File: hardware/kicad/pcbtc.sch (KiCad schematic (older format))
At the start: 93 parts, among them J1 USB_C_Receptacle_USB2.0, J4 XT60, Q2 LMG5200, Q3 IPD50R380CE, Q4 LMG5200, SW1 Setup, T1 Transformer_1P_1S_0, U1 USBLC6-4SC6, U10 74LVC1G11, U11 USBLC6-4SC6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

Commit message: pretty schematics
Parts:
- removed R17: 10, Resistor_SMD:R_0603_1608Metric, symbol Device:R
- added R17: 10, symbol Device:R_Small
- added R?: 5k1, Resistor_SMD:R_0603_1608Metric, symbol Device:R_Small
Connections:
- net GNDD: now also R?.2
- net at Q3.1 (G): now also R17.1
- net at U7.2 (GATE): now also R17.2
- net FLYBACK renamed BOOST
- net BOOST: now also R?.1
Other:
- note added: "DCDC feedback"
- note added: "Dead time generator"
- note added: "Feedback recovery"
- note added: "Flyback boost converter"
- note added: "GaN full bridge"
- note added: "STM32 control"
- note added: "USB Vin"
- note added: "USB current measurement"
- moved on the sheet: C1, C10, C11, C12, C13, C14, C15, C16, C17, C18, C19, C2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

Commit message: Released V1.6 gerber
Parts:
- removed JP1: Boot, Jumper:SolderJumper-2_P1.3mm_Open_RoundedPad1.0x1.5mm, symbol Jumper:SolderJumper_2_Open
- removed R7: 2k, Resistor_SMD:R_0603_1608Metric, symbol Device:R
- added C32: 10u, Capacitor_SMD:C_0603_1608Metric, symbol Device:C_Small
- added C33, C40: 10u, Capacitor_SMD:C_1206_3216Metric, symbol Device:C
- added C39, C42: 470pF, Capacitor_SMD:C_1206_3216Metric, symbol Device:C
- added C41: 100n, Capacitor_SMD:C_1206_3216Metric, symbol Device:C
- added C43, C44: 10u, Capacitor_SMD:C_0603_1608Metric, symbol Device:C
- added R15: 120, Resistor_SMD:R_0603_1608Metric, symbol Device:R
- C34: value 1n -> 100n; footprint Capacitor_SMD:C_0603_1608Metric -> Capacitor_SMD:C_1206_3216Metric
- JP2: footprint Jumper:SolderJumper-3_P1.3mm_Open_RoundedPad1.0x1.5mm -> Jumper:SolderJumper-3_P1.3mm_Bridged12_RoundedPad1.0x1.5mm
- R17: footprint (none) -> Resistor_SMD:R_0603_1608Metric
- T1: value Transformer_1P_1S_0 -> WE 750032052
- U7: symbol 000my_lib:MIC4416 -> pcbtc-rescue:MIC4416-000my_lib
- gave numbers to parts that had none: 1
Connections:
- net +5V: now also R15.1; no longer U11.5 (VBUS)
- net GND: now also C43.2, C44.1
- net GNDD: now also C32.2, C33.2, C39.2, C40.2, C41.2, C42.2
- net VBUS: now also C34.1, C33.1, C39.1, C40.1, C41.1, C42.1
- net BOOT0: now reaches U4.44 (BOOT0)
- net BOOT0: now also C35.1, R26.1, SW1.2, U4.17 (PA7); no longer C34.1
- net at C5.1, L1.1, Q2.6 (VCC): now also C43.1
- net at C4.2, L2.1, Q4.6 (VCC): now also C44.2
- new net: C32.1, R15.2, U11.5 (VBUS)
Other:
- moved on the sheet: H1, R10

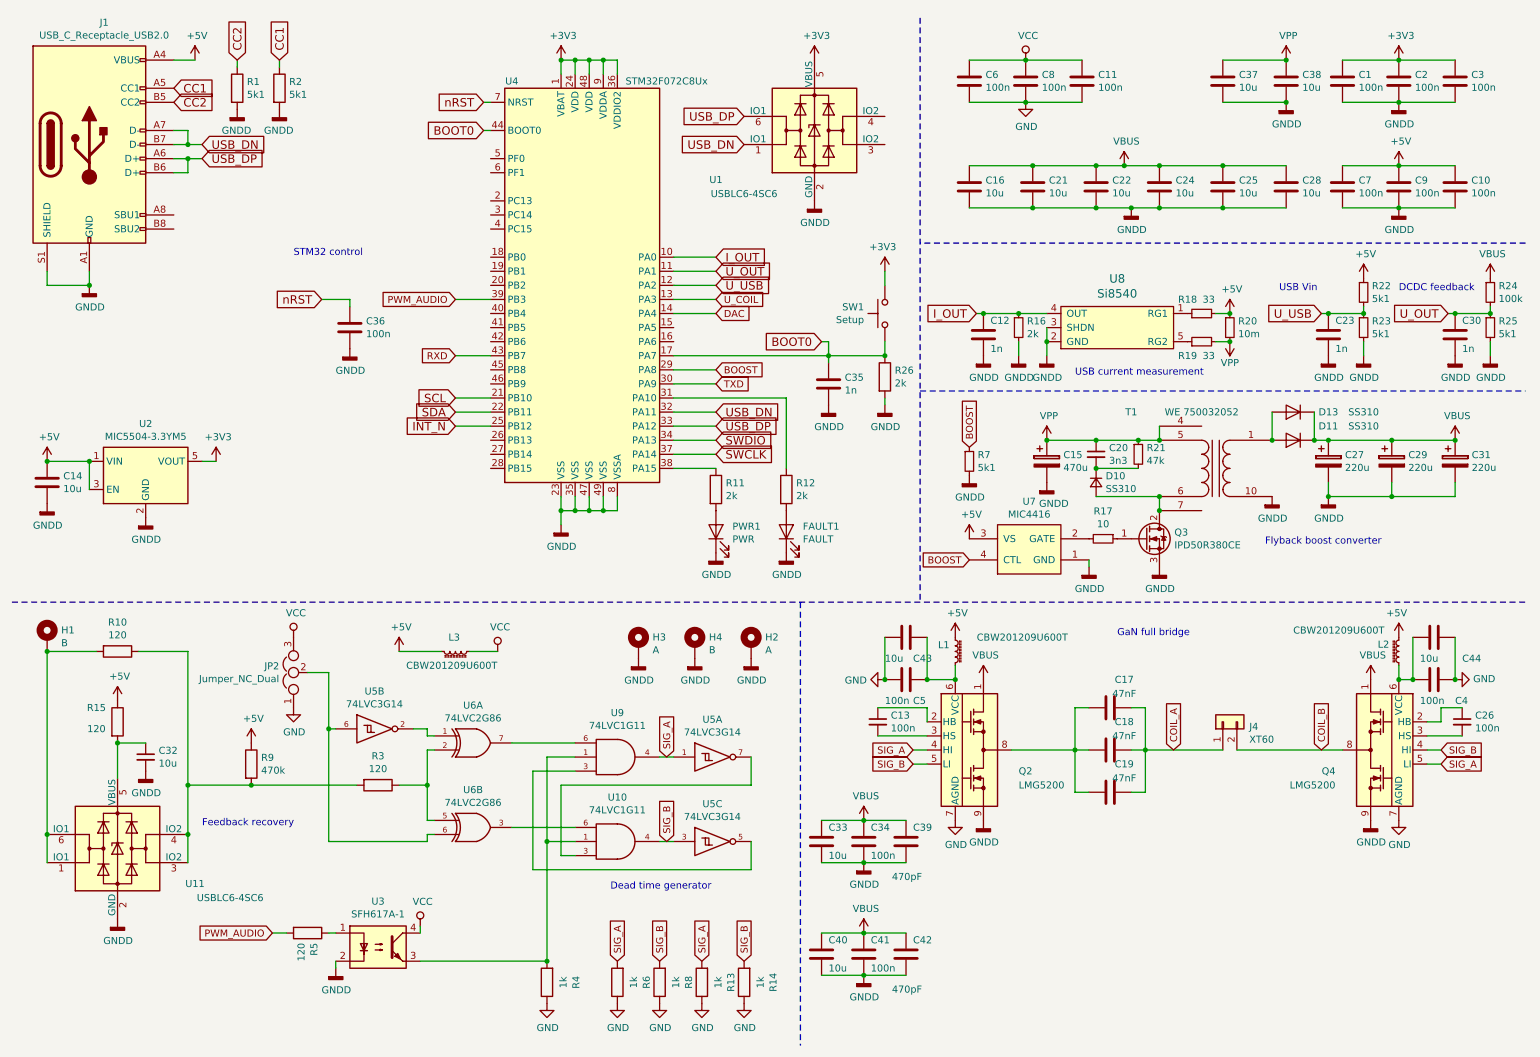
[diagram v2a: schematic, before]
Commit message: FIX: interactive html bom capacitor values
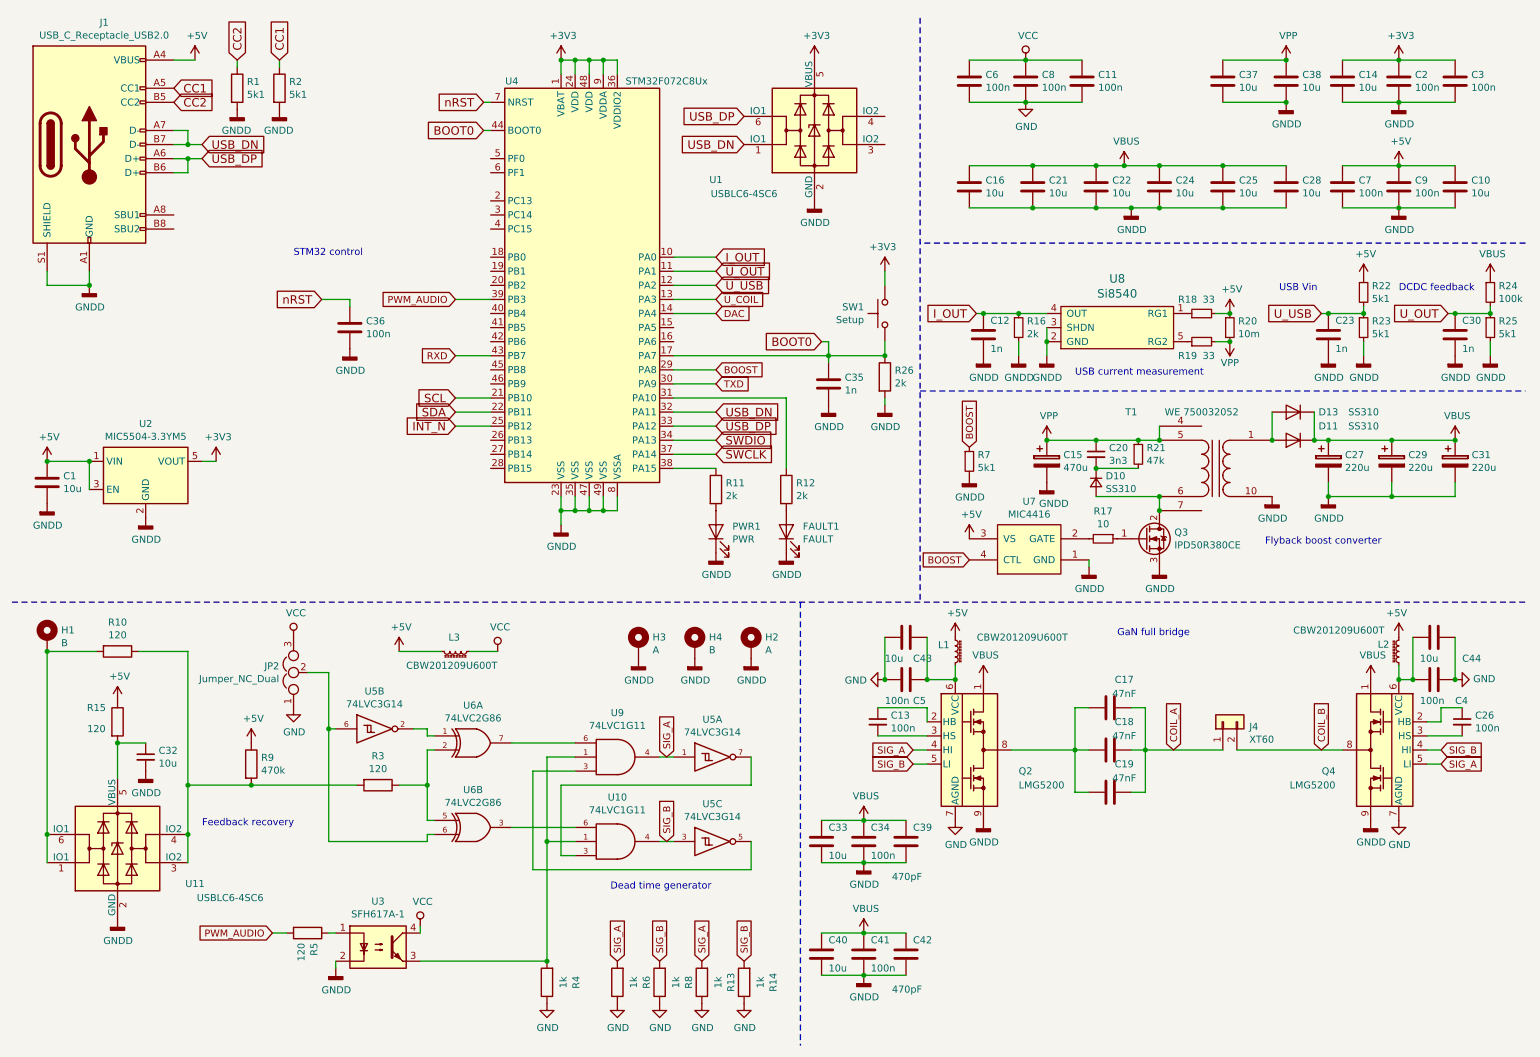
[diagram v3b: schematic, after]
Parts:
- C10: value 100n -> 10u
- C14: renamed from C1; value 100n -> 10u
- renumbered C14 to C1
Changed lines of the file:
@@
 $EndComp
 $Comp
-L Device:C C14
+L Device:C C1
 U 1 1 5BF19DA3
 P 700 3800
-F 0 "C14" H 815 3846 50  0000 L CNN
+F 0 "C1" H 815 3846 50  0000 L CNN
 F 1 "10u" H 815 3755 50  0000 L CNN
 F 2 "Capacitor_SMD:C_1206_3216Metric" H 738 3650 50  0001 C CNN
@@
 $EndComp
 $Comp
-L Device:C C1
+L Device:C C14
 U 1 1 5A9C143E
 P 9900 950
-F 0 "C1" H 10015 996 50  0000 L CNN
-F 1 "100n" H 10015 905 50  0000 L CNN
+F 0 "C14" H 10015 996 50  0000 L CNN
+F 1 "10u" H 10015 905 50  0000 L CNN
 F 2 "Capacitor_SMD:C_0603_1608Metric" H 9938 800 50  0001 C CNN
 F 3 "~" H 9900 950 50  0001 C CNN
@@
 P 10700 1700
 F 0 "C10" H 10815 1746 50  0000 L CNN
-F 1 "100n" H 10815 1655 50  0000 L CNN
+F 1 "10u" H 10815 1655 50  0000 L CNN
 F 2 "Capacitor_SMD:C_0603_1608Metric" H 10738 1550 50  0001 C CNN
 F 3 "~" H 10700 1700 50  0001 C CNN
